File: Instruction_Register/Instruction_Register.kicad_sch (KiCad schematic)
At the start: 22 parts, among them U7 74LS245, U8 74LS173, U9 74LS173

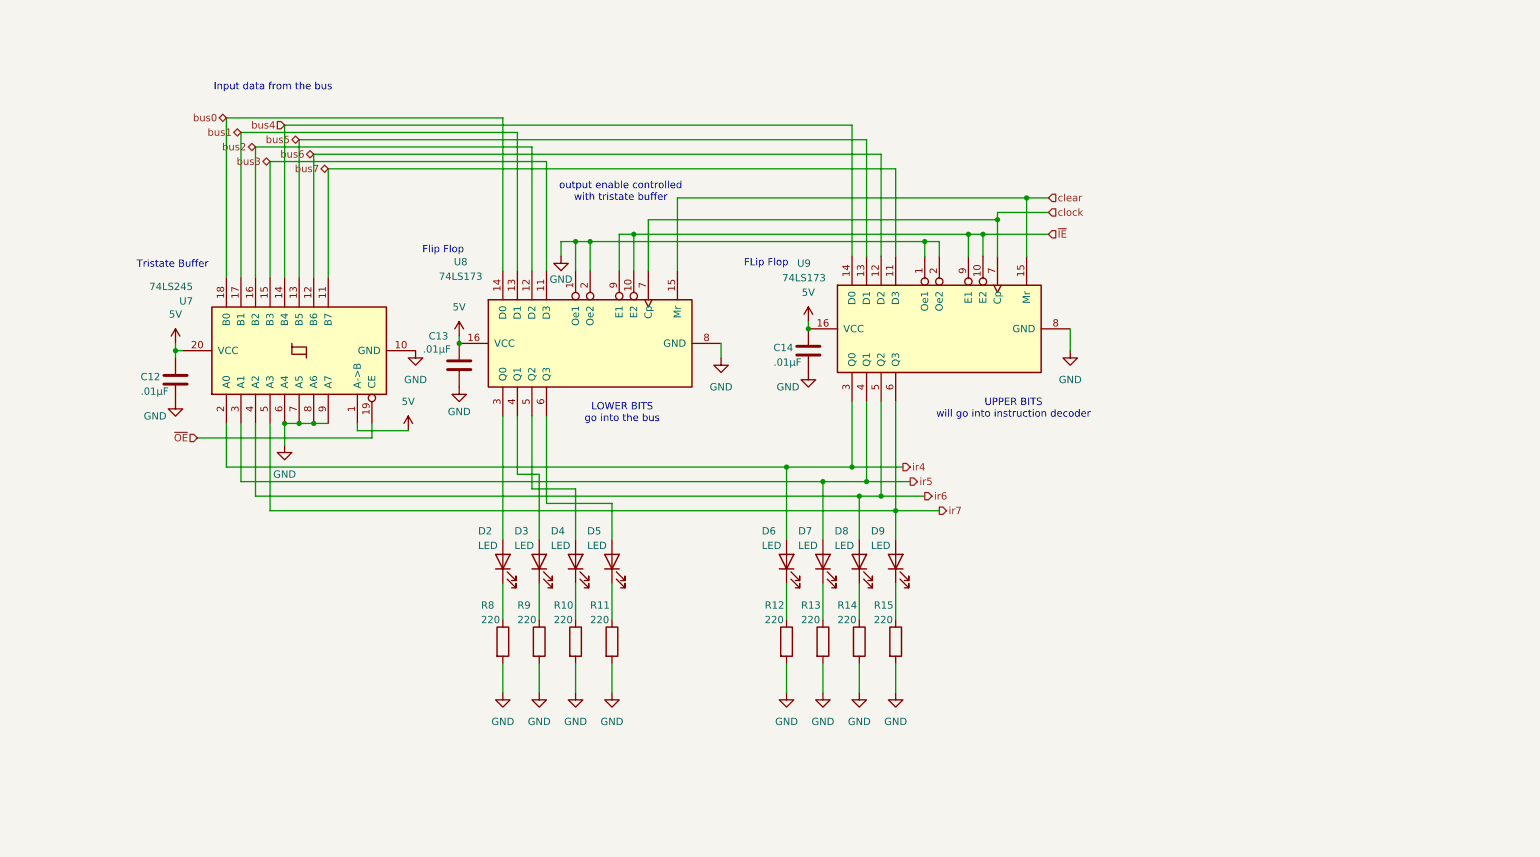
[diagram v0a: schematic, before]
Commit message: mostly routed IR, fixed logic issue in Clock Module
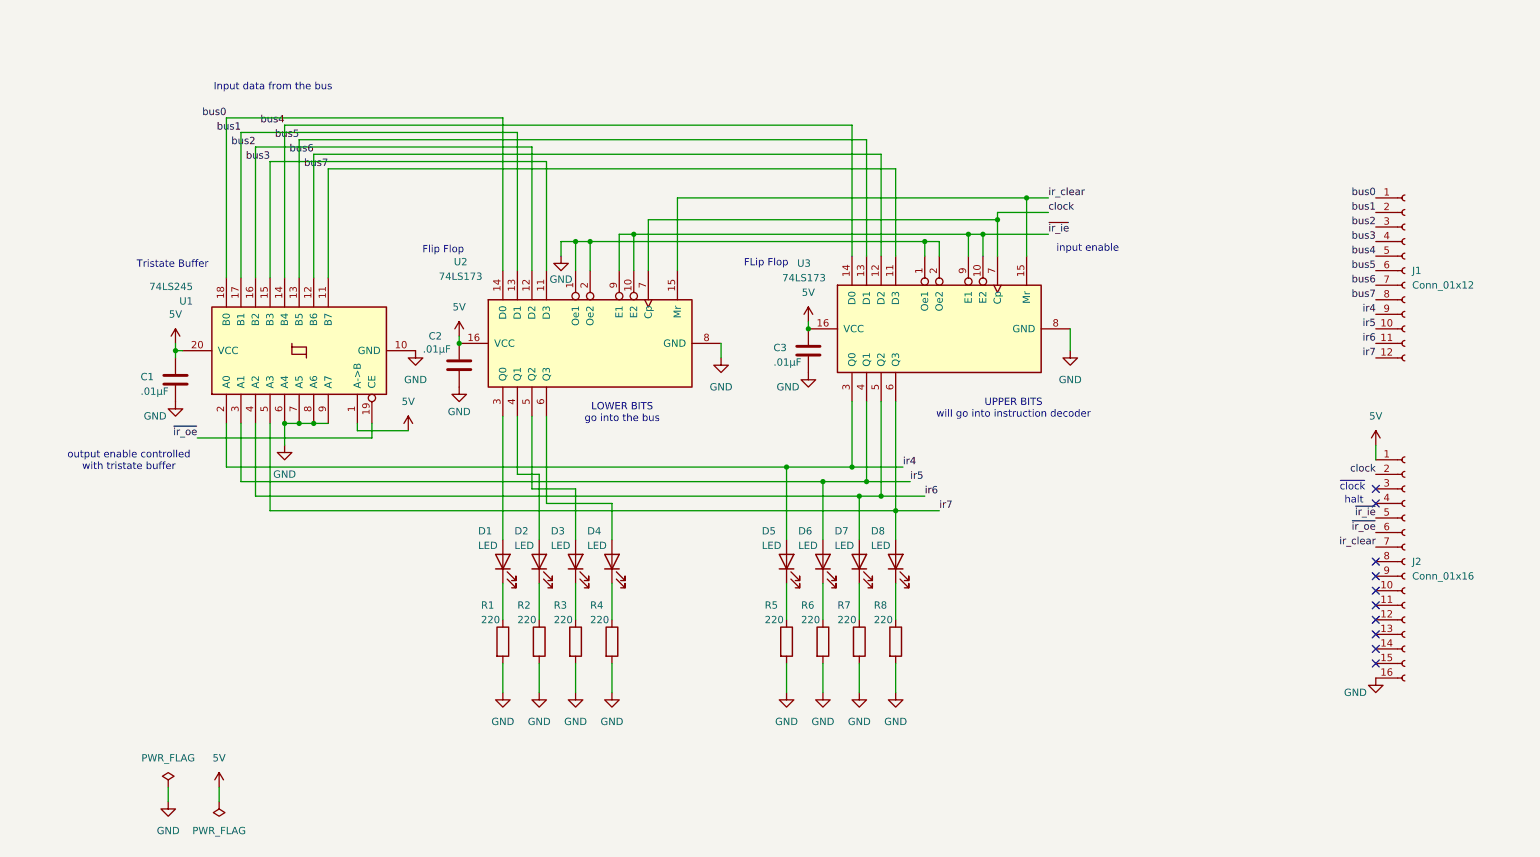
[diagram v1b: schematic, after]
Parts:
- added J1: Conn_01x12, Connector_PinSocket_2.54mm:PinSocket_1x12_P2.54mm_Vertical, symbol Connector:Conn_01x12_Socket
- added J2: Conn_01x16, Connector_PinSocket_2.54mm:PinSocket_1x16_P2.54mm_Vertical, symbol Connector:Conn_01x16_Socket
- renumbered C12 to C1, C13 to C2, C14 to C3, D2 to D1, D3 to D2, D4 to D3, D5 to D4, D6 to D5, D7 to D6, D8 to D7, D9 to D8, R8 to R1, R9 to R2, R10 to R3, R11 to R4, R12 to R5, R13 to R6, R14 to R7, R15 to R8, U7 to U1, U8 to U2, U9 to U3
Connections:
- net 5V: now also J2.1 (Pin_1)
- net GND: now also J2.16 (Pin_16)
- net bus0: now also J1.1 (Pin_1)
- net bus1: now also J1.2 (Pin_2)
- net bus2: now also J1.3 (Pin_3)
- net bus3: now also J1.4 (Pin_4)
- net bus4: now also J1.5 (Pin_5)
- net bus5: now also J1.6 (Pin_6)
- net bus6: now also J1.7 (Pin_7)
- net bus7: now also J1.8 (Pin_8)
- net clock: now also J2.2 (Pin_2)
- net ir4: now also J1.9 (Pin_9)
- net ir5: now also J1.10 (Pin_10)
- net ir6: now also J1.11 (Pin_11)
- net ir7: now also J1.12 (Pin_12)
- net clear renamed ir_clear
- net ir_clear: now also J2.7 (Pin_7)
- net ~{IE} renamed ~{ir_ie}
- net ~{ir_ie}: now also J2.5 (Pin_5)
- net ~{OE} renamed ~{ir_oe}
- net ~{ir_oe}: now also J2.6 (Pin_6)
- no-connect marks 0 -> 10
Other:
- note added: "halt"
- note added: "input enable"
- note added: "~{clock}"

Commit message: returning to pc104 standard
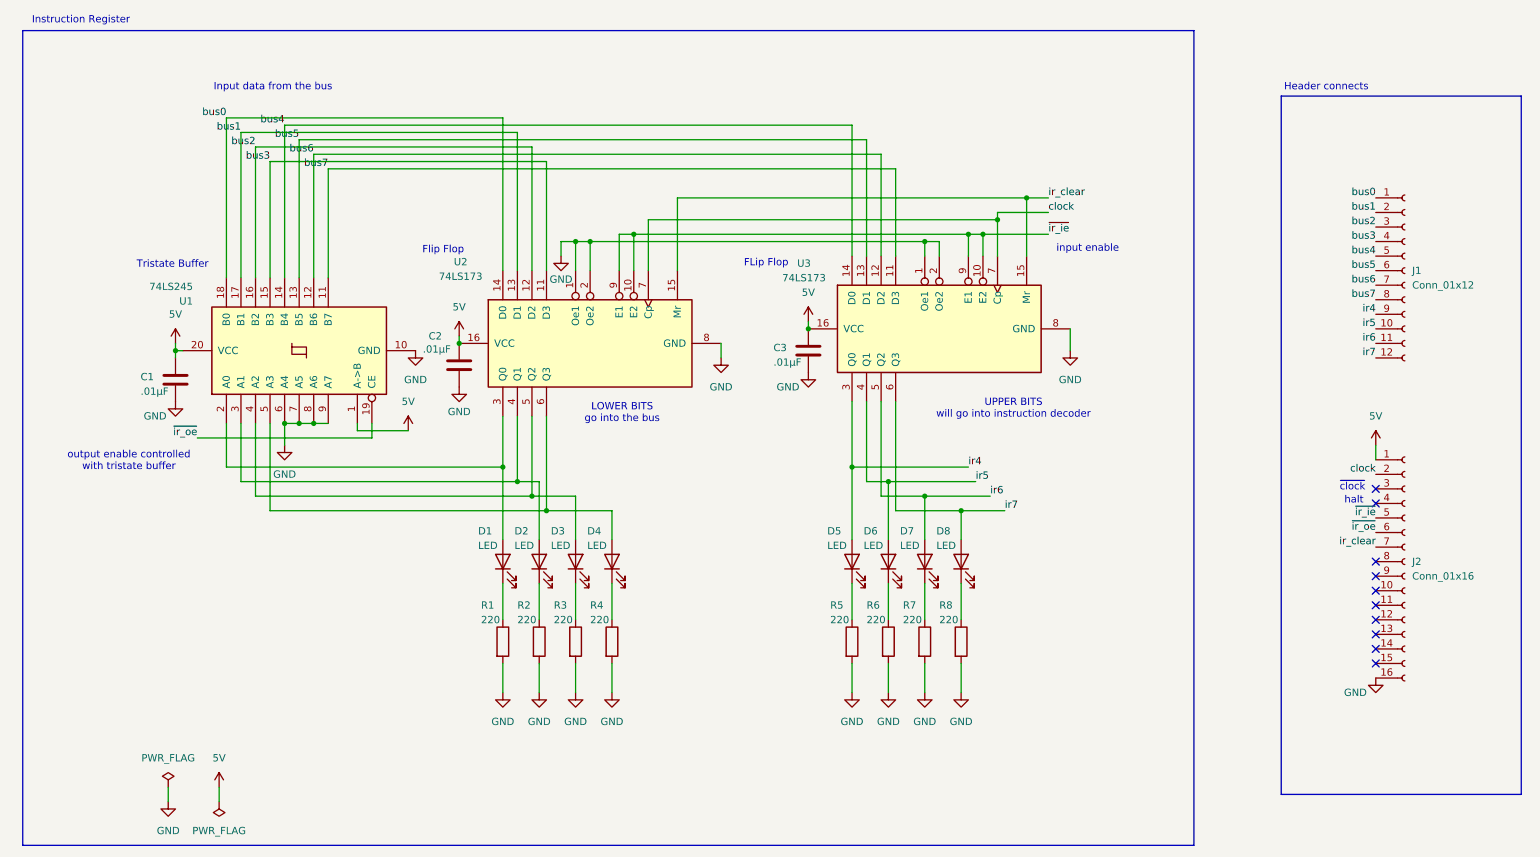
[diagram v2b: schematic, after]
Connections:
- net ir4: no longer U1.2 (A0)
- net ir5: no longer U1.3 (A1)
- net ir6: no longer U1.4 (A2)
- net ir7: no longer U1.5 (A3)
- net at D2.2 (A), U2.4 (Q1): now also U1.3 (A1)
- net at D3.2 (A), U2.5 (Q2): now also U1.4 (A2)
- net at D4.2 (A), U2.6 (Q3): now also U1.5 (A3)
- net at D1.2 (A), U2.3 (Q0): now also U1.2 (A0)
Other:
- note added: "Header connects"
- note added: "Instruction Register"
- company: (none) -> Arsenal Gear
- title: (none) -> Instruction Register
- moved on the sheet: D5, D6, D7, D8, R5, R6, R7, R8

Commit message: updated instruction register to match pc104
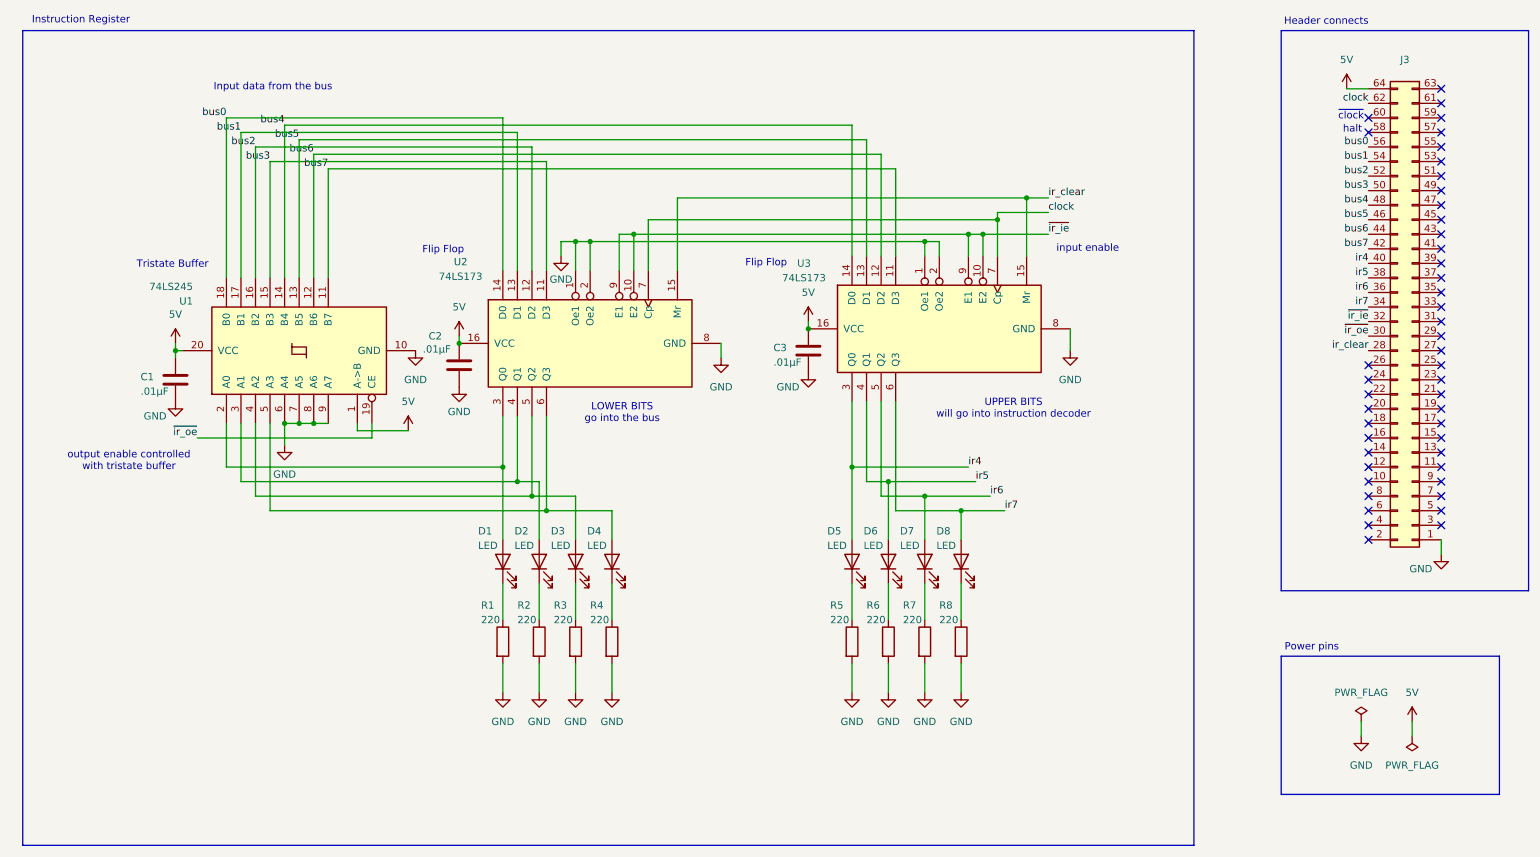
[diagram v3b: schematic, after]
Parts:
- removed J1: Conn_01x12, Connector_PinSocket_2.54mm:PinSocket_1x12_P2.54mm_Vertical, symbol Connector:Conn_01x12_Socket
- removed J2: Conn_01x16, Connector_PinSocket_2.54mm:PinSocket_1x16_P2.54mm_Vertical, symbol Connector:Conn_01x16_Socket
- added J3: ~, MyFootPrints:PC104-Standard, symbol pc104:PC104
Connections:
- net 5V: now also J3.64
- net GND: now also J3.1
- net bus0: now also J3.56
- net bus1: now also J3.54
- net bus2: now also J3.52
- net bus3: now also J3.50
- net bus4: now also J3.48
- net bus5: now also J3.46
- net bus6: now also J3.44
- net bus7: now also J3.42
- net clock: now also J3.62
- net ir4: now also J3.40
- net ir5: now also J3.38
- net ir6: now also J3.36
- net ir7: now also J3.34
- net ir_clear: now also J3.28
- net ~{ir_ie}: now also J3.32
- net ~{ir_oe}: now also J3.30
- no-connect marks 10 -> 46
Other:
- note added: "Power pins"
- note removed: "FLip Flop"

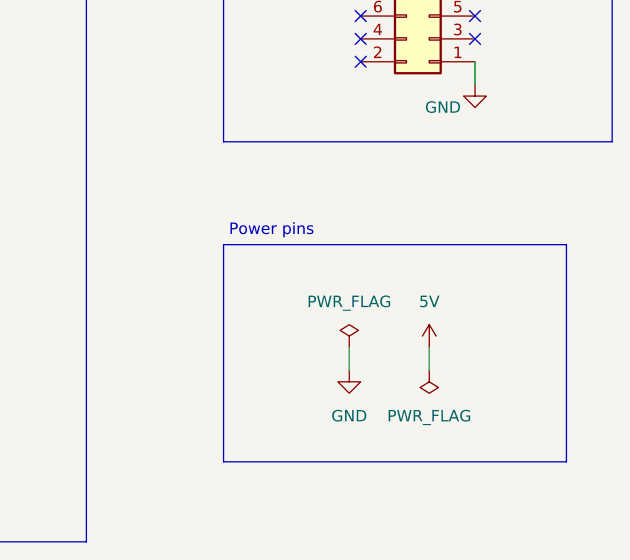
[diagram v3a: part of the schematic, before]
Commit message: updated Arithemetic Logic Unit
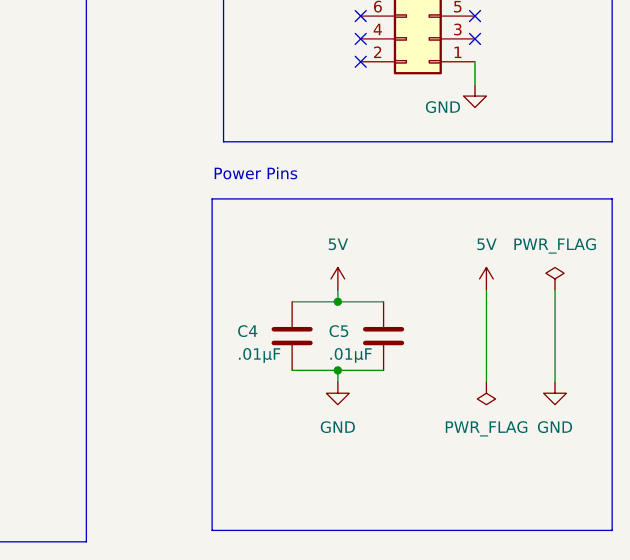
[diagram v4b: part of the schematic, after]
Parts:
- added C4, C5: .01µF, Capacitor_THT:C_Disc_D5.0mm_W2.5mm_P2.50mm, symbol Device:C
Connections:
- net 5V: now also C4.2, C5.2
- net GND: now also C4.1, C5.1
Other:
- note added: "Power Pins"
- note removed: "Power pins"
